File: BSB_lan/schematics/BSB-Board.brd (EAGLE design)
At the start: 29.7 x 53.3 mm, 18 parts, among them Q1 BC107, X1 SSW-106-02-S-S, X2 SSW-116-02-S-S

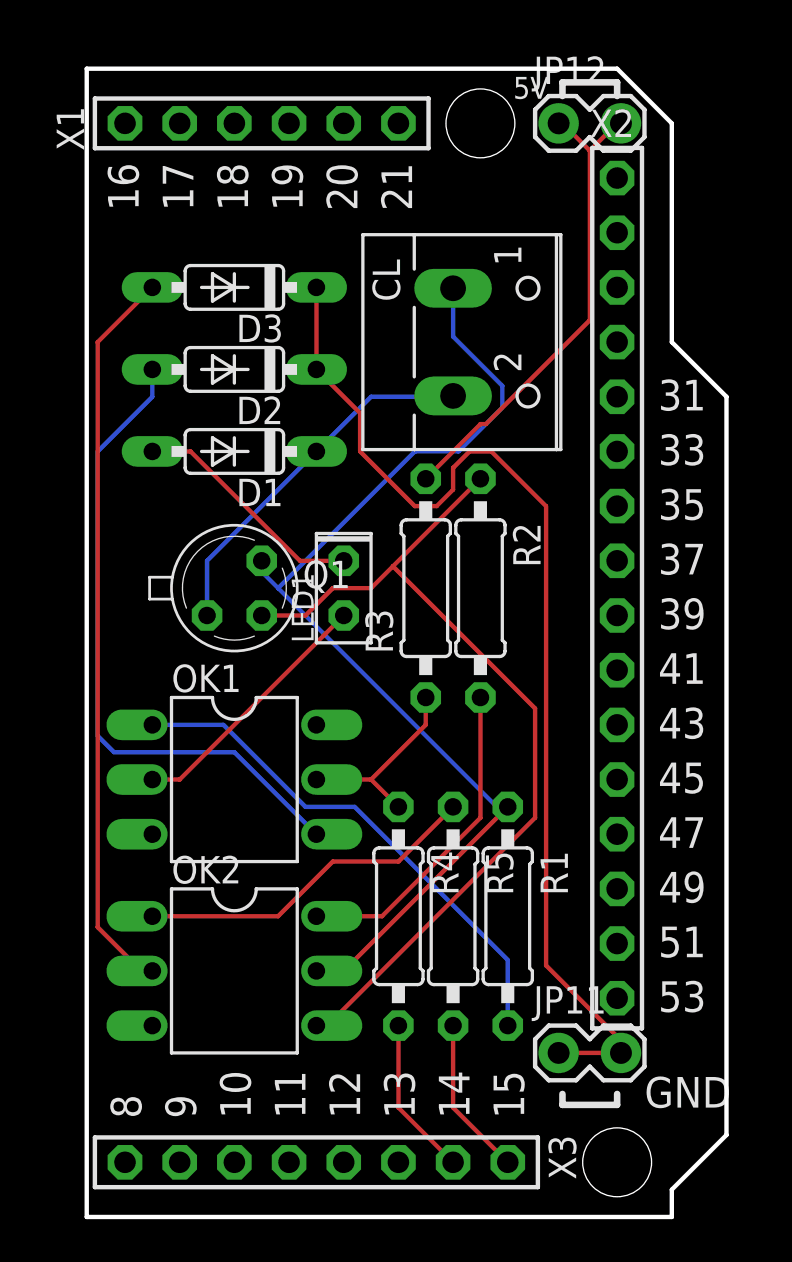
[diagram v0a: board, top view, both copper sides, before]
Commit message: Add files via upload
Schematic:
- fix ERC warnings in schematic (missing junctions - use NET instead of WIRE).
Board:
- rearrange components
- use thicker wires
- route single-sided

TODO:
- use smaller packages for diodes (they are 1N4148!)
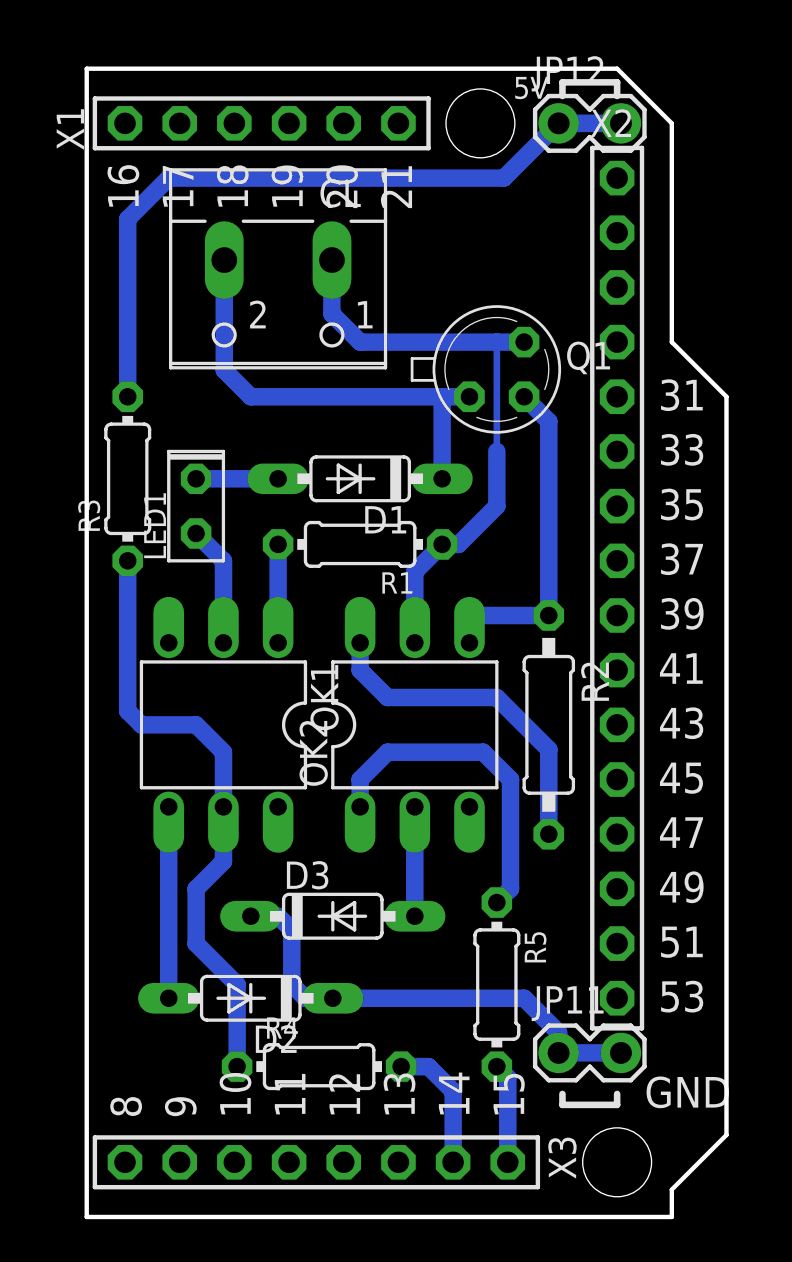
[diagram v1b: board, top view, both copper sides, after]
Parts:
- R1, R3, R4, R5: device eagle-ltspice:0207/10 -> eagle-ltspice:0204/7
- moved D3 29.6 mm to (11.4, 14.0), turned to 0 degrees
- moved D2 29.2 mm to (7.62, 10.2)
- moved R1 18.6 mm to (12.7, 31.2), turned to 180 degrees
- moved Q1 15.9 mm to (19.1, 39.4)
- moved R3 14.7 mm to (1.91, 34.3)
- moved OK2 14.2 mm to (15.2, 22.9), turned to 0 degrees
- moved CL 9.74 mm to (8.89, 43.2), turned to 180 degrees
- moved R4 7.90 mm to (10.8, 6.99), turned to 0 degrees
- moved LED1 7.85 mm to (5.08, 33.0)
- moved R2 7.10 mm to (21.5, 22.9)
- moved D1 5.98 mm to (12.7, 34.3)
- moved R5 3.77 mm to (19.1, 10.8)
- moved OK1 2.59 mm to (6.35, 22.9), turned to 180 degrees
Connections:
- net N$10 renamed GND
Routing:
- net N$13: track 34.2 -> 5.08 mm
- net GND: track 50.5 -> 21.9 mm
- net N$5: track 41.4 -> 15.6 mm
- net N$9: track 30.1 -> 8.89 mm
- net N$6: track 48.9 -> 28.0 mm
- net N$1: track 24.1 -> 4.57 mm
- net N$8: track 9.20 -> 28.1 mm
- net N$14: track 22.5 -> 33.0 mm
- net N$4: track 11.0 -> 3.81 mm
- net N$2: track 12.0 -> 5.61 mm
- net N$7: track 17.2 -> 20.8 mm
- net A15: track 7.40 -> 4.66 mm
- net A14: track 7.40 -> 6.19 mm
- net N$11: track 16.1 -> 15.3 mm
